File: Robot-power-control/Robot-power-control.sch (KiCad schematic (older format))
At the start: 37 parts, among them J1 Conn_01x02, J10 Conn_01x02, J2 Conn_01x02, J3 Conn_01x06, J4 Conn_01x02, J5 Conn_01x02, J6 Conn_01x02, J7 Conn_01x02, J8 Conn_01x02, J9 Conn_01x02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

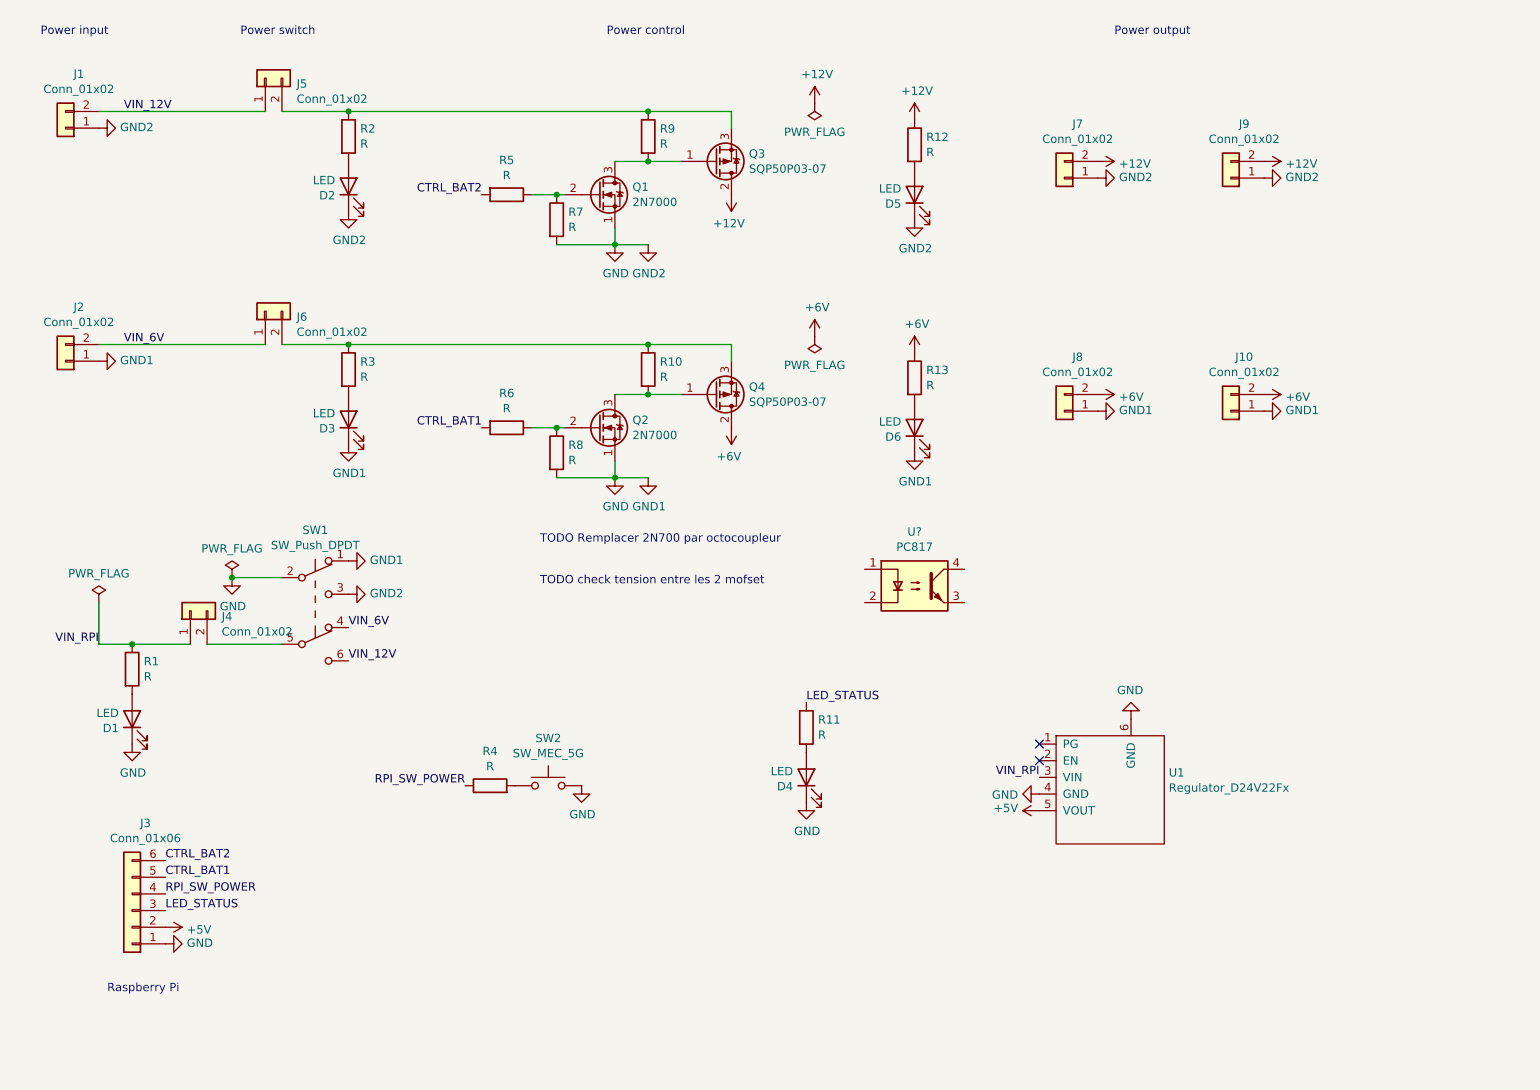
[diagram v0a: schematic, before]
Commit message: Update Robot-power-control - PCB command
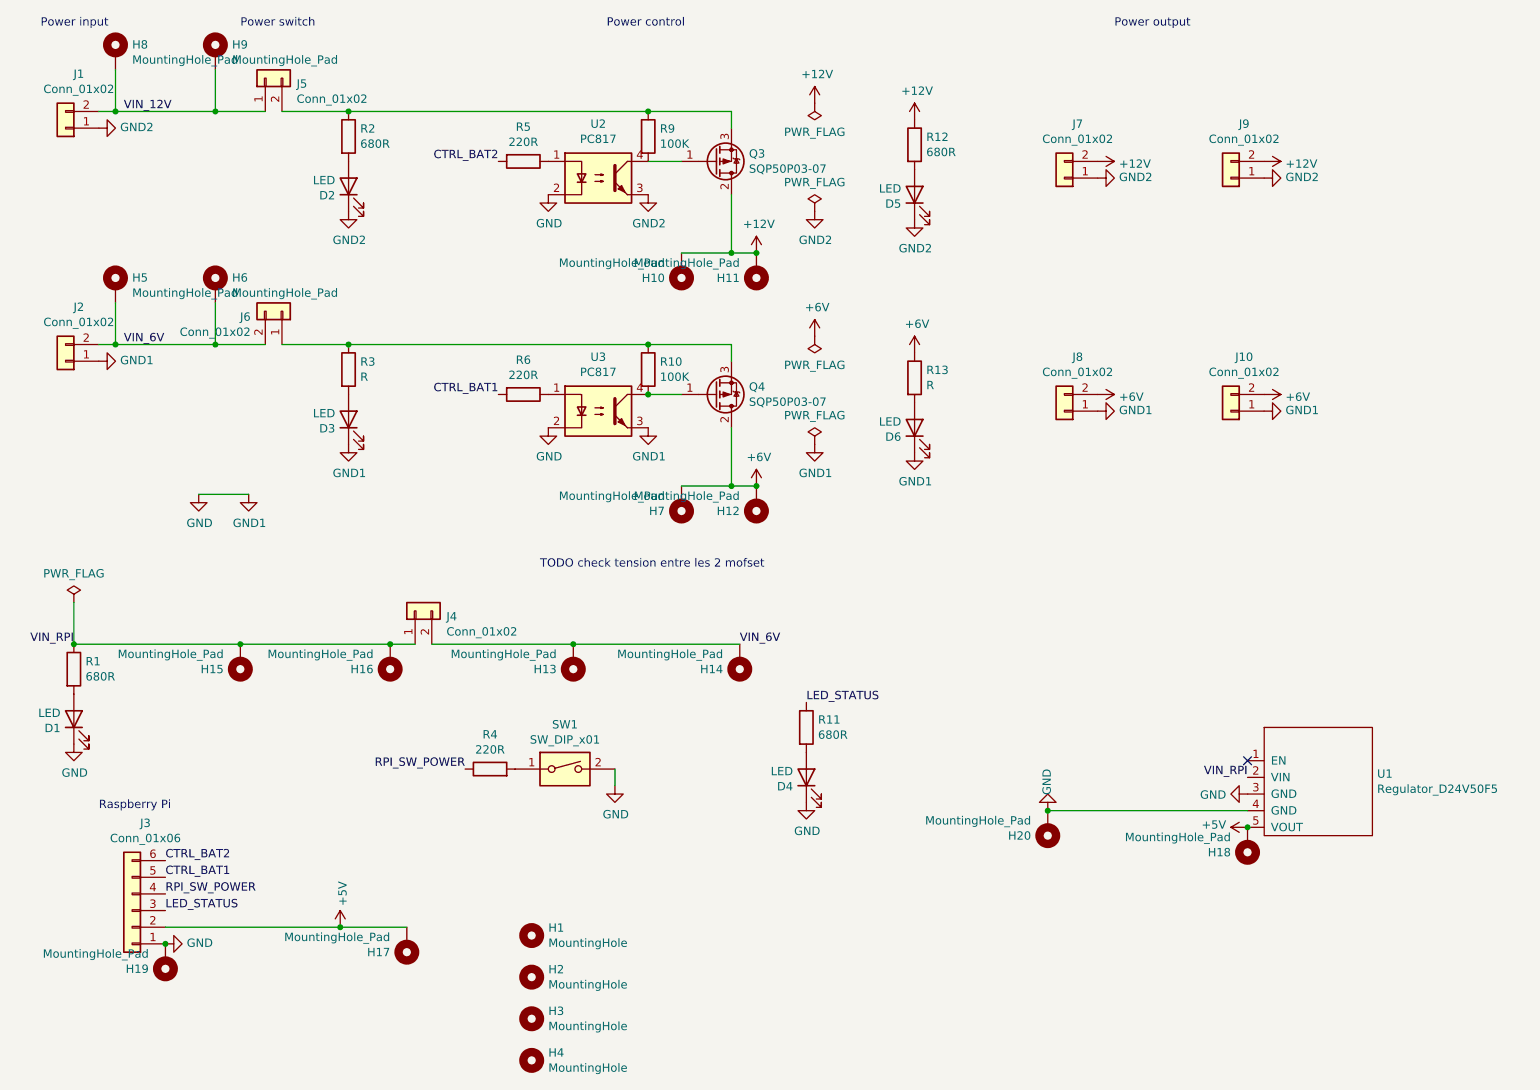
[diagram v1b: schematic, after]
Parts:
- removed Q1, Q2: 2N7000, Package_TO_SOT_THT:TO-92_Inline, symbol Transistor_FET:2N7000
- removed R7, R8: R, symbol Device:R
- removed SW1: SW_Push_DPDT, symbol Switch:SW_Push_DPDT
- removed SW2: SW_MEC_5G, symbol Switch:SW_MEC_5G
- removed U1: Regulator_D24V22Fx, symbol Pololu:Regulator_D24V22Fx
- added H1, H2, H3, H4: MountingHole, MountingHole:MountingHole_3.2mm_M3, symbol Mechanical:MountingHole
- added H10, H11, H12, H5, H6, H7, H8, H9: MountingHole_Pad, MountingHole:MountingHole_1.5mm_Pad, symbol Mechanical:MountingHole_Pad
- added H13, H14, H15, H16, H17, H18, H19, H20: MountingHole_Pad, MountingHole:MountingHole_1.0mm_Pad, symbol Mechanical:MountingHole_Pad
- added SW1: SW_DIP_x01, Button_Switch_THT:SW_PUSH_6mm_H9.5mm, symbol Switch:SW_DIP_x01
- added U1: Regulator_D24V50F5, Pololu:Pololu_reg15d, symbol Pololu:Regulator_D24V50F5
- added U2: PC817, Package_DIP:DIP-4_W7.62mm, symbol Isolator:PC817
- D1, D2, D3, D4, D5, D6: footprint (none) -> LED_THT:LED_D5.0mm
- J1, J10, J2, J4, J5, J6, J7, J8, J9: footprint (none) -> Connector_Molex:Molex_Micro-Fit_3.0_43650-0215_1x02_P3.00mm_Vertical
- J3: footprint (none) -> Connector_Molex:Molex_SL_171971-0006_1x06_P2.54mm_Vertical
- R1, R11, R12, R2: value R -> 680R; footprint (none) -> Resistor_THT:R_Axial_DIN0207_L6.3mm_D2.5mm_P7.62mm_Horizontal
- R10, R9: value R -> 100K; footprint (none) -> Resistor_THT:R_Axial_DIN0207_L6.3mm_D2.5mm_P7.62mm_Horizontal
- R13, R3: footprint (none) -> Resistor_THT:R_Axial_DIN0207_L6.3mm_D2.5mm_P7.62mm_Horizontal
- R4, R5, R6: value R -> 220R; footprint (none) -> Resistor_THT:R_Axial_DIN0207_L6.3mm_D2.5mm_P7.62mm_Horizontal
- gave numbers to parts that had none: 1
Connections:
- net +12V: now also H10.1, H11.1
- net +5V: now also H17.1, H18.1, U1.5 (VOUT)
- net +6V: now also H12.1, H7.1
- net GND: now also U3.2, U3.3, H19.1, H20.1, SW1.2, U1.3 (GND), U1.4 (GND), U2.2; no longer D2.1 (K), D5.1 (K), J1.1 (Pin_1), J7.1 (Pin_1), J9.1 (Pin_1)
- net VIN_12V: now also H8.1, H9.1
- net VIN_6V: now also J4.2 (Pin_2), J6.2 (Pin_2), H13.1, H14.1, H5.1, H6.1; no longer J6.1 (Pin_1)
- net VIN_RPI: now also H15.1, H16.1, U1.2 (VIN)
- net at Q4.1 (G), R10.2: now also U3.4
- net at Q4.3 (S), R10.1, R3.1: now also J6.1 (Pin_1); no longer J6.2 (Pin_2)
- net at R6.1: now also U3.1
- net at Q3.1 (G), R9.2: now also U2.4
- net at R5.1: now also U2.1
- net at R4.2: now also SW1.1
- new net GND2: D2.1 (K), D5.1 (K), J1.1 (Pin_1), J7.1 (Pin_1), J9.1 (Pin_1), U2.3
- no-connect marks 2 -> 1
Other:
- note removed: "TODO Remplacer 2N700 par octocoupleur"
- moved on the sheet: D1, J4, R1, R4, R5, R6, U3
